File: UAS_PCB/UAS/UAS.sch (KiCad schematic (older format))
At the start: 17 parts, among them J1 SM02B-PASS-TBT, J2 SM02B-PASS-TBT, J3 SM02B-PASS-TBT, J4 SM02B-PASS-TBT, U1 JST-7-Pin, U10 UAS-rescue_7.5V-2.4A-Converte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, U11 JST-3-Pin, U12 Signal-Pad, U13 Signal-Pad, U2 5A-5V-Converter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

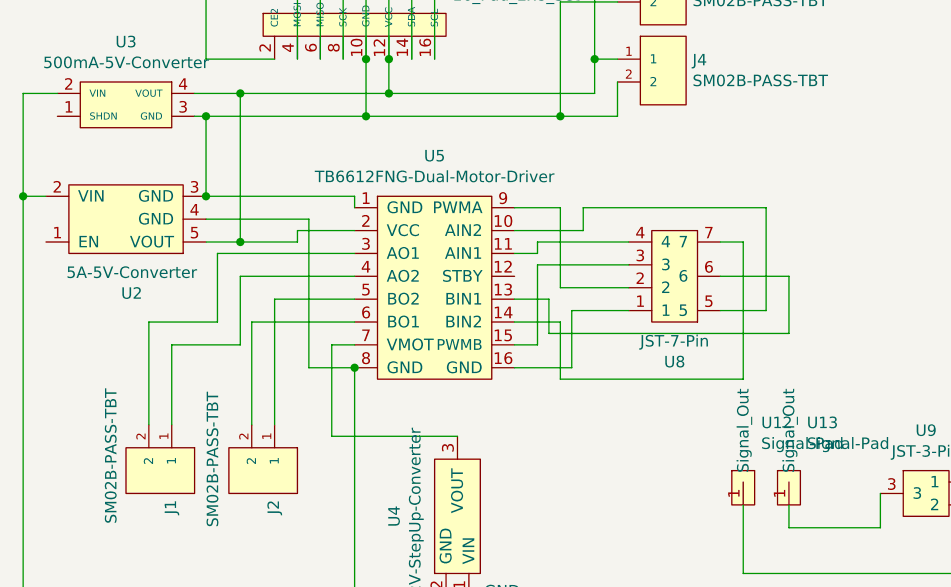
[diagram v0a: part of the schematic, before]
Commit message: slight rearranging and pin changes, PCS connector on top still needs to be reorganized for a straight shot
also, for gods sake we gotta change the symbols for connectors on the diagram
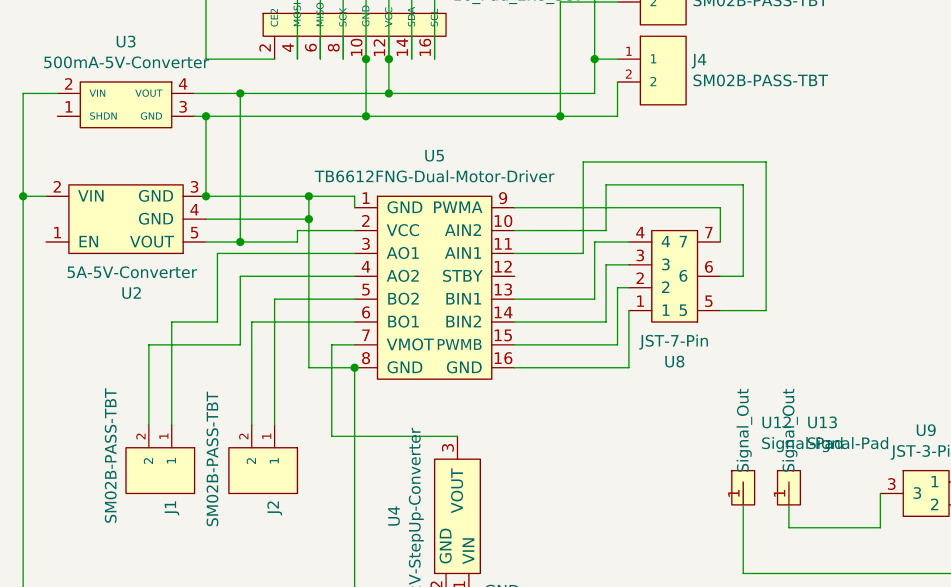
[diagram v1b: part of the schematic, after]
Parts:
- U4: footprint UAS:Pololu_12V_Step_Up_Voltage_Regulator -> UAS:Pololu_12V_Step_Up_Voltage_Regulator_SMT
- U5: footprint UAS:Pololu_TB6612_Dual_Motor_Driver_Carrier -> UAS:Pololu_TB6612_Dual_Motor_Driver_Carrier_SMT
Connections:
- net GND: now also J3.2, J4.2, U2.3 (GND), U3.3 (GND), U5.1 (GND), U6.10 (GND), U6.9 (GND)
- net at U8.2: now also U5.15 (PWMB); no longer U5.9 (PWMA)
- net at U8.3: now also U5.14 (BIN2); no longer U5.15 (PWMB)
- net at U8.4: now also U5.13 (BIN1); no longer U5.11 (AIN1)
- net at U8.5: now also U5.11 (AIN1); no longer U5.10 (AIN2)
- net at U8.6: now also U5.10 (AIN2); no longer U5.13 (BIN1)
- net at U8.7: now also U5.9 (PWMA); no longer U5.14 (BIN2)
- net at U5.3 (AO1): now also J1.1; no longer J1.2
- net at U5.4 (AO2): now also J1.2; no longer J1.1

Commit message: fixed connector, 12v trace needs to be bigger for sure , probably close to 1.5mm
symbols are still messy FeelsBadMan
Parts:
- U6: value 16_Pad_2x8_Set -> 16_Pad_2x8_Set-UAS-cache; symbol UAS-rescue:16_Pad_2x8_Set-UAS-cache -> UAS-rescue:UAS-rescue_16_Pad_2x8_Set-UAS-cache-UAS-cache
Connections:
- net GND: now also U6.13 (GND), U6.14 (GND); no longer U6.10 (GND), U6.9 (GND)
- net +12V: now reaches U10.3 (VIN), U2.2 (VIN), U3.2 (VIN), U4.1 (VIN), U7.1
- net +5V: now reaches J3.1, J4.1, U2.5 (VOUT), U3.4 (VOUT), U5.2 (VCC)
- net +5V: now also U6.15 (VCC), U6.16 (VCC); no longer U6.11 (VCC), U6.12 (VCC)
- net +7.5V: now reaches U10.5 (VOUT), U11.2, U9.2
- new net: U1.6, U6.10 (SDA), U6.9 (SDA)
- new net: U1.7, U6.11 (SCL), U6.12 (SCL)
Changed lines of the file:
@@
 	1850 3800 2050 3800
 Wire Wire Line
-	2050 3800 2050 4450
+	2050 3800 2050 4050
 Wire Wire Line
 	2050 4450 1900 4450
@@
 	1100 4250 1100 6400
 Wire Wire Line
-	1100 6400 2750 6400
+	1100 6400 2650 6400
 Connection ~ 1100 4250
 Connection ~ 2750 6400
@@
 	2350 5000 2550 5000
 Connection ~ 2550 5000
-Wire Wire Line
-	1900 3900 2600 3900
-Wire Wire Line
-	2600 3900 2600 3650
 Connection ~ 1900 3900
-Wire Wire Line
-	2050 3800 2700 3800
-Wire Wire Line
-	2700 3800 2700 3650
 Connection ~ 2050 3800
 Wire Wire Line
-	2200 3650 1900 3650
-Wire Wire Line
-	1900 3650 1900 2500
-Wire Wire Line
-	1900 2500 2300 2500
-Wire Wire Line
-	2200 3250 2000 3250
-Wire Wire Line
-	2000 3250 2000 2600
-Wire Wire Line
-	2000 2600 2300 2600
-Wire Wire Line
-	2300 2700 2200 2700
-Wire Wire Line
-	2200 2700 2200 2400
-Wire Wire Line
-	2200 2400 2300 2400
-Wire Wire Line
-	2400 2800 2100 2800
-Wire Wire Line
-	2100 2800 2100 2300
-Wire Wire Line
-	2100 2300 2300 2300
-Wire Wire Line
-	2500 2800 2700 2800
-Wire Wire Line
-	2700 2800 2700 2600
-Wire Wire Line
-	2800 2450 2700 2450
-Wire Wire Line
-	2900 2300 2700 2300
-Wire Wire Line
 	3700 3900 3700 3750
-Connection ~ 2600 3900
-Wire Wire Line
-	2700 3800 3600 3800
-Connection ~ 2700 3800
 Wire Wire Line
 	3600 3300 3700 3300
@@
 	6000 6000 6000 5600
 Connection ~ 5350 5600
-Wire Wire Line
-	2800 2450 2800 3250
-Wire Wire Line
-	2900 2300 2900 3250
-Wire Wire Line
-	2300 2700 2300 3250
-Wire Wire Line
-	2400 2800 2400 3250
-Wire Wire Line
-	2500 2800 2500 3250
-$Comp
-L UAS-rescue:16_Pad_2x8_Set-UAS-cache U6
-U 1 1 6040B9AA
-P 2550 3050
-F 0 "U6" H 2978 2821 50  0000 L CNN
-F 1 "16_Pad_2x8_Set" H 2978 2730 50  0000 L CNN
-F 2 "UAS:16_Pad_Set_2mm_pitch" H 2550 3050 50  0001 C CNN
-F 3 "" H 2550 3050 50  0001 C CNN
-	1    2550 3050
-	1    0    0    -1
-$EndComp
-Wire Wire Line
-	2300 3650 2300 3250
-Connection ~ 2300 3250
-Wire Wire Line
-	2400 3650 2400 3250
-Connection ~ 2400 3250
-Wire Wire Line
-	2500 3650 2500 3250
-Connection ~ 2500 3250
-Wire Wire Line
-	2800 3650 2800 3250
-Connection ~ 2800 3250
-Wire Wire Line
-	2600 3250 2600 3650
-Connection ~ 2600 3650
-Wire Wire Line
-	2600 3900 3450 3900
-Wire Wire Line
-	2700 3250 2700 3650
-Connection ~ 2700 3650
-Wire Wire Line
-	2900 3650 2900 3250
-Connection ~ 2900 3250
 $Comp
 L UAS-rescue:Signal-Pad-UAS-cache U12
@@
 Wire Wire Line
 	2350 4250 2550 4250
+$Comp
+L power:+12V #PWR0102
+U 1 1 603B00E9
+P 2650 6400
+F 0 "#PWR0102" H 2650 6250 50  0001 C CNN
+F 1 "+12V" H 2665 6573 50  0000 C CNN
+F 2 "" H 2650 6400 50  0001 C CNN
+F 3 "" H 2650 6400 50  0001 C CNN
+	1    2650 6400
+	1    0    0    -1
+$EndComp
+Connection ~ 2650 6400
+Wire Wire Line
+	2650 6400 2750 6400
+$Comp
+L power:+5V #PWR0103
+U 1 1 603B0FAA
+P 2050 4050
+F 0 "#PWR0103" H 2050 3900 50  0001 C CNN
+F 1 "+5V" V 2065 4178 50  0000 L CNN
+F 2 "" H 2050 4050 50  0001 C CNN
+F 3 "" H 2050 4050 50  0001 C CNN
+	1    2050 4050
+	0    1    1    0
+$EndComp
+Connection ~ 2050 4050
+Wire Wire Line
+	2050 4050 2050 4450
+$Comp
+L power:+7.5V #PWR0104
+U 1 1 603BC06C
+P 5350 6000
+F 0 "#PWR0104" H 5350 5850 50  0001 C CNN
+F 1 "+7.5V" V 5365 6128 50  0000 L CNN
+F 2 "" H 5350 6000 50  0001 C CNN
+F 3 "" H 5350 6000 50  0001 C CNN
+	1    5350 6000
+	0    -1   -1   0
+$EndComp
+Connection ~ 5350 6000
+Wire Wire Line
+	1900 3900 2800 3900
+Wire Wire Line
+	2050 3800 2900 3800
+Wire Wire Line
+	2500 3650 2500 3250
+Wire Wire Line
+	2600 3650 2600 3250
+Wire Wire Line
+	2700 3650 2700 3250
+$Comp
+L UAS-rescue:UAS-rescue_16_Pad_2x8_Set-UAS-cache-UAS-cache U6
+U 1 1 6040B9AA
+P 2550 3050
+F 0 "U6" H 2978 2821 50  0000 L CNN
+F 1 "16_Pad_2x8_Set-UAS-cache" H 2978 2730 50  0000 L CNN
+F 2 "UAS:16_Pad_Set_2mm_pitch" H 2550 3050 50  0001 C CNN
+F 3 "" H 2550 3050 50  0001 C CNN
+	1    2550 3050
+	1    0    0    -1
+$EndComp
+Wire Wire Line
+	2300 3250 2300 3650
+Wire Wire Line
+	2400 3250 2400 3650
+Wire Wire Line
+	2300 2600 2100 2600
+Wire Wire Line
+	2100 2600 2100 3250
+Wire Wire Line
+	2100 3250 2200 3250
+Wire Wire Line
+	2300 2500 2000 2500
+Wire Wire Line
+	2000 2500 2000 3650
+Wire Wire Line
+	2000 3650 2200 3650
+Wire Wire Line
+	2300 3250 2300 2950
+Wire Wire Line
+	2300 2950 2200 2950
+Wire Wire Line
+	2200 2950 2200 2400
+Wire Wire Line
+	2200 2400 2300 2400
+Connection ~ 2300 3250
+Wire Wire Line
+	2400 3250 2400 2900
+Wire Wire Line
+	2400 2900 2150 2900
+Wire Wire Line
+	2150 2900 2150 2300
+Wire Wire Line
+	2150 2300 2300 2300
+Connection ~ 2400 3250
+Wire Wire Line
+	2500 3250 2500 2750
+Wire Wire Line
+	2500 2750 2700 2750
+Wire Wire Line
+	2700 2750 2700 2600
+Connection ~ 2500 3250
+Wire Wire Line
+	2600 3250 2600 2850
+Wire Wire Line
+	2600 2850 2800 2850
+Wire Wire Line
+	2800 2850 2800 2450
+Wire Wire Line
+	2800 2450 2700 2450
+Connection ~ 2600 3250
+Wire Wire Line
+	2700 3250 2700 2950
+Wire Wire Line
+	2700 2950 2900 2950
+Wire Wire Line
+	2900 2950 2900 2300
+Wire Wire Line
+	2900 2300 2700 2300
+Connection ~ 2700 3250
+Wire Wire Line
+	2900 3250 2900 3650
+Connection ~ 2900 3800
+Wire Wire Line
+	2900 3800 3600 3800
+Connection ~ 2900 3650
+Wire Wire Line
+	2900 3650 2900 3800
+Wire Wire Line
+	2800 3250 2800 3650
+Connection ~ 2800 3900
+Wire Wire Line
+	2800 3900 3450 3900
+Connection ~ 2800 3650
+Wire Wire Line
+	2800 3650 2800 3900
 $EndSCHEMATC

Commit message: final version with kyles passthrough pads and graphics
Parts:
- added U14, U15, U16, U17: UAS-rescue_Signal-Pad-UAS-cache, UAS:Individual_Solder_Pad, symbol UAS-cache:UAS-rescue_Signal-Pad-UAS-cache
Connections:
- new net: U14.1 (Signal_Out), U15.1 (Signal_Out)
- new net: U16.1 (Signal_Out), U17.1 (Signal_Out)
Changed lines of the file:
@@
 Wire Wire Line
 	2800 3650 2800 3900
+$Comp
+L UAS-cache:UAS-rescue_Signal-Pad-UAS-cache U17
+U 1 1 603DAF7F
+P 5600 3750
+F 0 "U17" H 5512 3916 50  0000 R CNN
+F 1 "UAS-rescue_Signal-Pad-UAS-cache" H 5512 4007 50  0000 R CNN
+F 2 "UAS:Individual_Solder_Pad" H 5600 3750 50  0001 C CNN
+F 3 "" H 5600 3750 50  0001 C CNN
+	1    5600 3750
+	-1   0    0    1
+$EndComp
+$Comp
+L UAS-cache:UAS-rescue_Signal-Pad-UAS-cache U15
+U 1 1 603D9E61
+P 5300 3750
+F 0 "U15" H 5212 3916 50  0000 R CNN
+F 1 "UAS-rescue_Signal-Pad-UAS-cache" H 5212 4007 50  0000 R CNN
+F 2 "UAS:Individual_Solder_Pad" H 5300 3750 50  0001 C CNN
+F 3 "" H 5300 3750 50  0001 C CNN
+	1    5300 3750
+	-1   0    0    1
+$EndComp
+$Comp
+L UAS-cache:UAS-rescue_Signal-Pad-UAS-cache U16
+U 1 1 603D9324
+P 5600 3350
+F 0 "U16" H 5678 3609 50  0000 L CNN
+F 1 "UAS-rescue_Signal-Pad-UAS-cache" H 5678 3518 50  0000 L CNN
+F 2 "UAS:Individual_Solder_Pad" H 5600 3350 50  0001 C CNN
+F 3 "" H 5600 3350 50  0001 C CNN
+	1    5600 3350
+	1    0    0    -1
+$EndComp
+$Comp
+L UAS-cache:UAS-rescue_Signal-Pad-UAS-cache U14
+U 1 1 603D8772
+P 5300 3350
+F 0 "U14" H 5378 3609 50  0000 L CNN
+F 1 "UAS-rescue_Signal-Pad-UAS-cache" H 5378 3518 50  0000 L CNN
+F 2 "UAS:Individual_Solder_Pad" H 5300 3350 50  0001 C CNN
+F 3 "" H 5300 3350 50  0001 C CNN
+	1    5300 3350
+	1    0    0    -1
+$EndComp
+Wire Wire Line
+	5300 3450 5300 3650
+Wire Wire Line
+	5600 3450 5600 3650
 $EndSCHEMATC

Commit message: change to different 3 pin connectors
the original ones were out of stock and the new ones are through hole and slightly longer, this required some shifting of parts. new version clears DRC and looks fine
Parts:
- U11, U9: footprint UAS:JST_SM03B-PASS-TBT(LF)(SN) -> UAS:JST_S03BPASK2LFSN
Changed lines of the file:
@@
 F 0 "U9" H 5050 5425 50  0000 C CNN
 F 1 "JST-3-Pin" H 5050 5334 50  0000 C CNN
-F 2 "UAS:JST_SM03B-PASS-TBT(LF)(SN)" H 5050 5450 50  0001 C CNN
+F 2 "UAS:JST_S03BPASK2LFSN" H 5050 5450 50  0001 C CNN
 F 3 "" H 5050 5450 50  0001 C CNN
 	1    5050 5350
@@
 F 0 "U11" H 5800 5425 50  0000 C CNN
 F 1 "JST-3-Pin" H 5800 5334 50  0000 C CNN
-F 2 "UAS:JST_SM03B-PASS-TBT(LF)(SN)" H 5800 5450 50  0001 C CNN
+F 2 "UAS:JST_S03BPASK2LFSN" H 5800 5450 50  0001 C CNN
 F 3 "" H 5800 5450 50  0001 C CNN
 	1    5800 5350

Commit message: swapped in the molex connectors and generated gerbers for this board
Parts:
- U11, U9: footprint UAS:JST_S03BPASK2LFSN -> UAS:MOLEX_SHDRRA3W50P0X200_1X3_0353630360
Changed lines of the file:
@@
 F 0 "U9" H 5050 5425 50  0000 C CNN
 F 1 "JST-3-Pin" H 5050 5334 50  0000 C CNN
-F 2 "UAS:JST_S03BPASK2LFSN" H 5050 5450 50  0001 C CNN
+F 2 "UAS:MOLEX_SHDRRA3W50P0X200_1X3_0353630360" H 5050 5450 50  0001 C CNN
 F 3 "" H 5050 5450 50  0001 C CNN
 	1    5050 5350
@@
 F 0 "U11" H 5800 5425 50  0000 C CNN
 F 1 "JST-3-Pin" H 5800 5334 50  0000 C CNN
-F 2 "UAS:JST_S03BPASK2LFSN" H 5800 5450 50  0001 C CNN
+F 2 "UAS:MOLEX_SHDRRA3W50P0X200_1X3_0353630360" H 5800 5450 50  0001 C CNN
 F 3 "" H 5800 5450 50  0001 C CNN
 	1    5800 5350
